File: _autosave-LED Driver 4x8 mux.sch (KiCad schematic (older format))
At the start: 23 parts, among them J1 Barrel_Jack_Switch, J2 Conn_01x02_Female, J3 8P8C_Shielded_x4, Q1 IRF9358TRPBF-2x_p-channel, Q2 IRF9358TRPBF-2x_p-channel, Q3 IRF9358TRPBF-2x_p-channel, Q4 IRF9358TRPBF-2x_p-channel, U1 SN74LV138AT_D_16, U2 TC4468EOE, U3 TC4468EOE

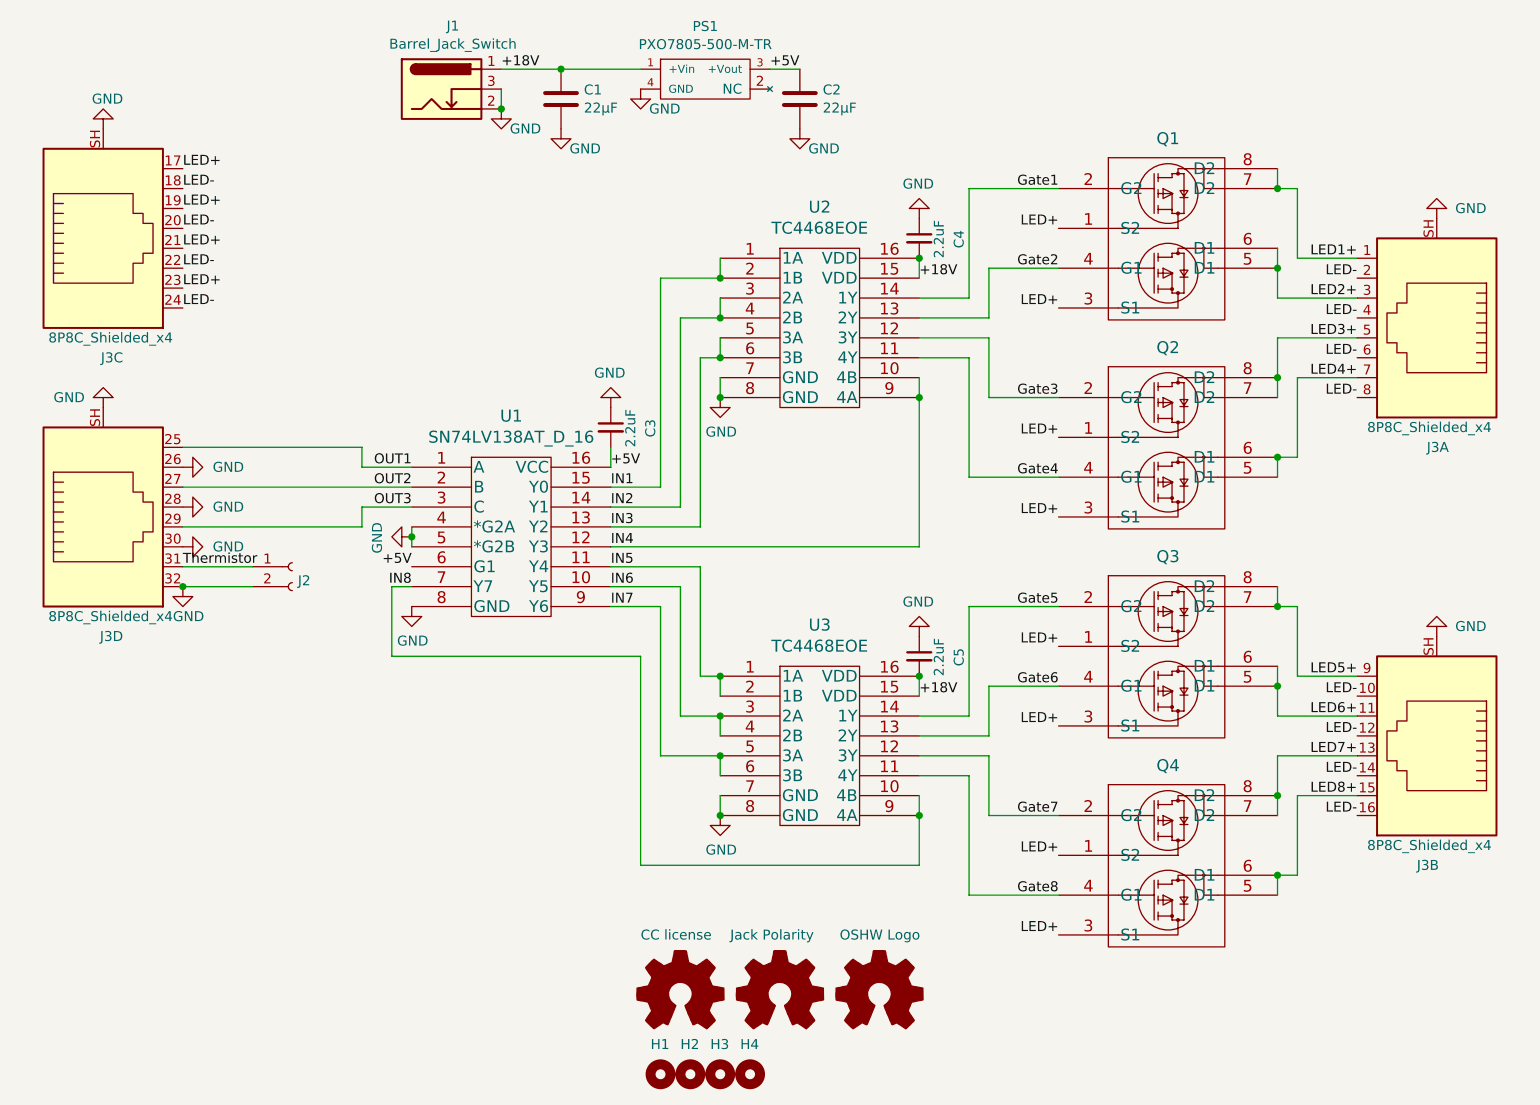
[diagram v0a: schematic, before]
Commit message: Board powered off LED river backup
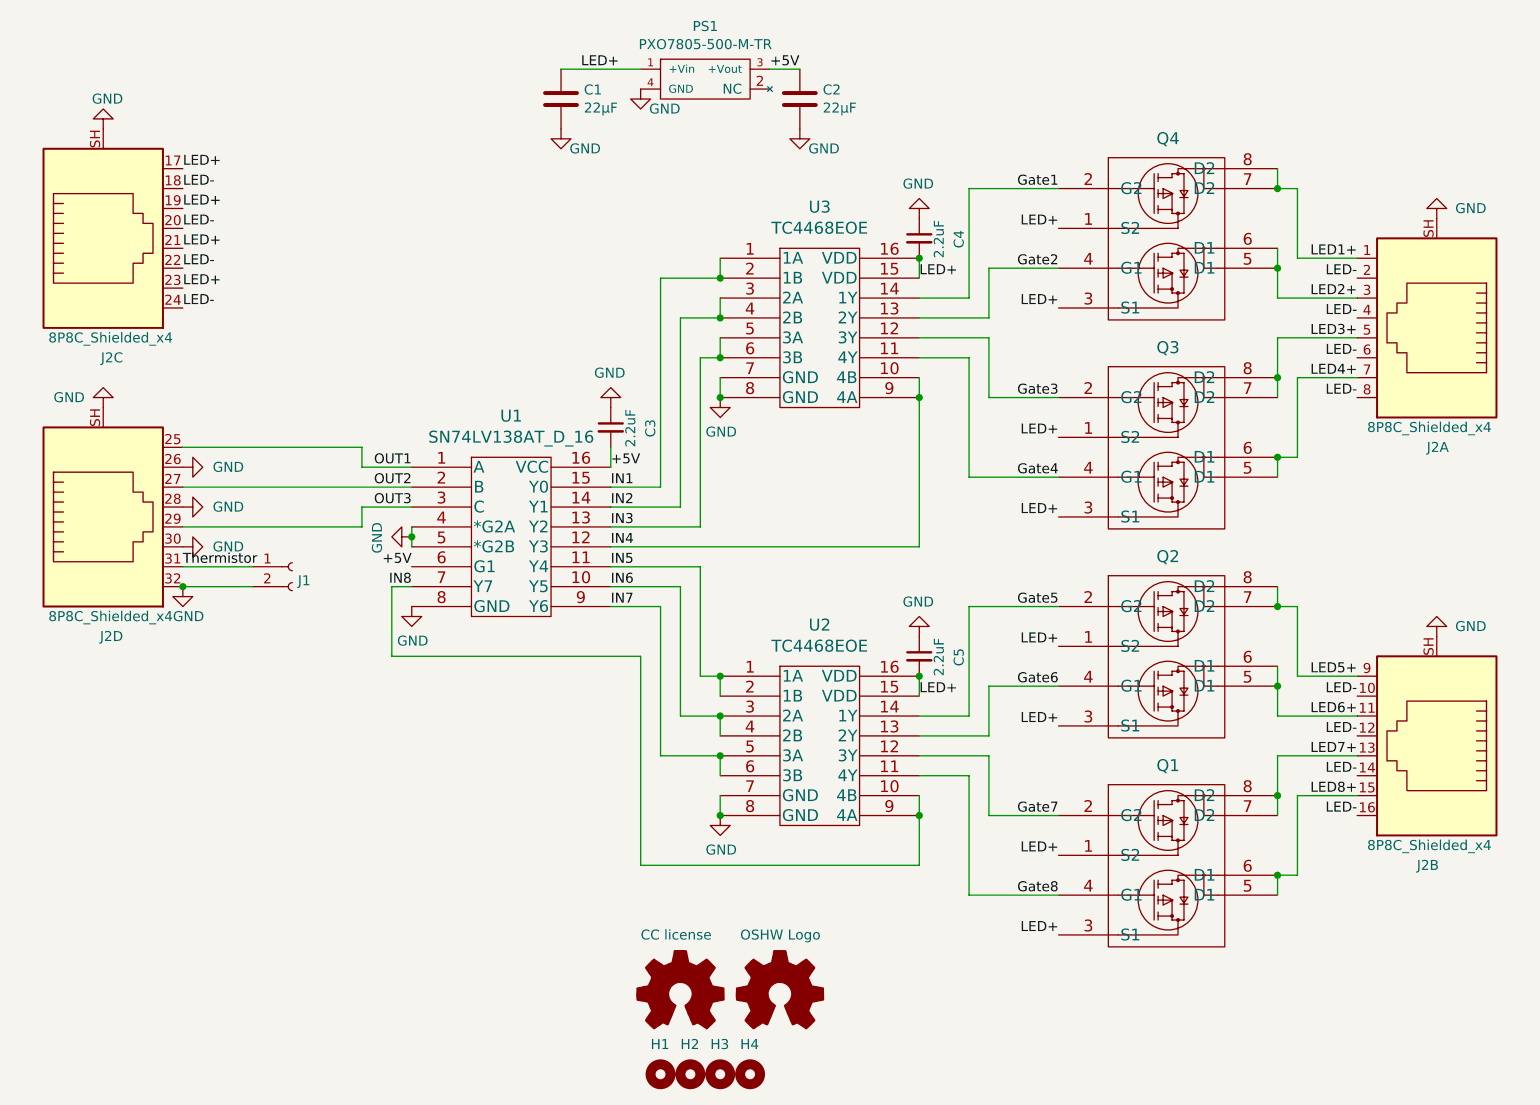
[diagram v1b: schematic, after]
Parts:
- removed J1: Barrel_Jack_Switch, Custom Footprints:DC-jack_54-00165, symbol Connector:Barrel_Jack_Switch
- removed LOGO2: Jack Polarity, Custom Footprints:Polarity_Center_Positive, symbol Graphic:Logo_Open_Hardware_Small
- J1: renamed from J2; value Conn_01x02_Female -> 2 pin header
- renumbered J3 to J2, Q4 to Q1, Q3 to Q2, Q2 to Q3, Q1 to Q4, U3 to U2, U2 to U3
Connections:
- net +18V is gone; now on net LED+: C1.1, C4.2, C5.2, PS1.1 (+Vin), U2.15 (VDD), U2.16 (VDD), U3.15 (VDD), U3.16 (VDD)
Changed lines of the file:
@@
 $EndComp
 $Comp
-L Custom_parts:8P8C_Shielded_x4 J3
+L Custom_parts:8P8C_Shielded_x4 J2
 U 4 1 5F58DBB9
 P 1150 5000
-F 0 "J3" H 1250 5650 50  0000 R CNN
+F 0 "J2" H 1250 5650 50  0000 R CNN
 F 1 "8P8C_Shielded_x4" H 1500 5550 50  0000 R CNN
 F 2 "Custom Footprints:RJ45_x4-RJSSE-5380-04" V 1150 5025 50  0001 C CNN
@@
 $EndComp
 $Comp
-L Custom_parts:8P8C_Shielded_x4 J3
+L Custom_parts:8P8C_Shielded_x4 J2
 U 3 1 5F57B5E3
 P 1150 3600
-F 0 "J3" H 1250 4250 50  0000 R CNN
+F 0 "J2" H 1250 4250 50  0000 R CNN
 F 1 "8P8C_Shielded_x4" H 1500 4150 50  0000 R CNN
 F 2 "Custom Footprints:RJ45_x4-RJSSE-5380-04" V 1150 3625 50  0001 C CNN
@@
 $EndComp
 $Comp
-L Custom_parts:8P8C_Shielded_x4 J3
+L Custom_parts:8P8C_Shielded_x4 J2
 U 2 1 5F589234
 P 7850 6150
-F 0 "J3" H 7950 6800 50  0000 R CNN
+F 0 "J2" H 7950 6800 50  0000 R CNN
 F 1 "8P8C_Shielded_x4" H 8200 6700 50  0000 R CNN
 F 2 "Custom Footprints:RJ45_x4-RJSSE-5380-04" V 7850 6175 50  0001 C CNN
@@
 $EndComp
 $Comp
-L Graphic:Logo_Open_Hardware_Small LOGO2
-U 1 1 5FF6ADDD
+L Graphic:Logo_Open_Hardware_Small LOGO3
+U 1 1 5FF6B1EE
 P 4550 7450
-F 0 "LOGO2" H 4550 7725 50  0001 C CNN
-F 1 "Jack Polarity" H 4300 7750 50  0000 L CNN
-F 2 "Custom Footprints:Polarity_Center_Positive" H 4550 7450 50  0001 C CNN
+F 0 "LOGO3" H 4550 7725 50  0001 C CNN
+F 1 "OSHW Logo" H 4350 7750 50  0000 L CNN
+F 2 "Symbol:OSHW-Logo2_7.3x6mm_SilkScreen" H 4550 7450 50  0001 C CNN
 F 3 "~" H 4550 7450 50  0001 C CNN
 	1    4550 7450
@@
 $EndComp
 $Comp
-L Graphic:Logo_Open_Hardware_Small LOGO3
-U 1 1 5FF6B1EE
-P 5050 7450
-F 0 "LOGO3" H 5050 7725 50  0001 C CNN
-F 1 "OSHW Logo" H 4850 7750 50  0000 L CNN
-F 2 "Symbol:OSHW-Logo2_7.3x6mm_SilkScreen" H 5050 7450 50  0001 C CNN
-F 3 "~" H 5050 7450 50  0001 C CNN
-	1    5050 7450
-	1    0    0    -1
-$EndComp
-$Comp
-L Custom_parts:8P8C_Shielded_x4 J3
+L Custom_parts:8P8C_Shielded_x4 J2
 U 1 1 5F5922AC
 P 7850 4050
-F 0 "J3" H 7900 4700 50  0000 R CNN
+F 0 "J2" H 7900 4700 50  0000 R CNN
 F 1 "8P8C_Shielded_x4" H 8200 4600 50  0000 R CNN
 F 2 "Custom Footprints:RJ45_x4-RJSSE-5380-04" V 7850 4075 50  0001 C CNN
@@
 	-1   0    0    1
 $EndComp
-Connection ~ 3150 3000
-Wire Wire Line
-	3150 2900 3150 3000
-$Comp
-L power:GND #PWR0108
-U 1 1 61A65F9D
-P 3150 3000
-F 0 "#PWR0108" H 3150 2750 50  0001 C CNN
-F 1 "GND" H 3350 2900 50  0000 R CNN
-F 2 "" H 3150 3000 50  0001 C CNN
-F 3 "" H 3150 3000 50  0001 C CNN
-	1    3150 3000
-	1    0    0    -1
-$EndComp
-$Comp
-L Connector:Barrel_Jack_Switch J1
-U 1 1 61A65FA5
-P 2850 2900
-F 0 "J1" H 2907 3217 50  0000 C CNN
-F 1 "Barrel_Jack_Switch" H 2907 3126 50  0000 C CNN
-F 2 "Custom Footprints:DC-jack_54-00165" H 2900 2860 50  0001 C CNN
-F 3 "https://tensility.s3-us-west-2.amazonaws.com/uploads/product_doc/document/4054/54-00165.pdf" H 2900 2860 50  0001 C CNN
-F 4 "Tensility International Corp" H 2850 2900 50  0001 C CNN "Manufacturer"
-F 5 "54-00165" H 2850 2900 50  0001 C CNN "Part #"
-	1    2850 2900
-	1    0    0    -1
-$EndComp
-Text Label 3150 2800 0    50   ~ 0
-+18V
 $Comp
 L power:GND #PWR015
@@
 $EndComp
 Wire Wire Line
-	3150 2800 3450 2800
-Wire Wire Line
 	3450 2800 3850 2800
-Connection ~ 3450 2800
 $Comp
 L power:GND #PWR0102
@@
 $EndComp
 $Comp
-L Custom_parts:TC4468EOE U2
+L Custom_parts:TC4468EOE U3
 U 1 1 64F06EE9
 P 4250 3750
-F 0 "U2" H 4750 4007 60  0000 C CNN
+F 0 "U3" H 4750 4007 60  0000 C CNN
 F 1 "TC4468EOE" H 4750 3901 60  0000 C CNN
 F 2 "Custom Footprints:TC4468EOE" H 5350 3990 60  0001 C CNN
@@
 Wire Wire Line
 	5250 5950 5250 5850
-Text Label 5250 3850 0    50   ~ 0
-+18V
-Text Label 5250 5950 0    50   ~ 0
-+18V
 Wire Wire Line
 	4250 6450 4250 6550
@@
 $EndComp
 $Comp
-L Custom_parts:IRF9358TRPBF-2x_p-channel Q1
+L Custom_parts:IRF9358TRPBF-2x_p-channel Q4
 U 1 1 64F4537D
 P 7450 3000
-F 0 "Q1" H 6500 2851 60  0000 C CNN
+F 0 "Q4" H 6500 2851 60  0000 C CNN
 F 1 "IRF9358TRPBF-2x_p-channel" H 6500 2875 60  0001 C CNN
 F 2 "Custom Footprints:IRF9358TRPBF-2x_p-channel" H 6500 2815 60  0001 C CNN
@@
 Gate8
 $Comp
-L Custom_parts:IRF9358TRPBF-2x_p-channel Q2
+L Custom_parts:IRF9358TRPBF-2x_p-channel Q3
 U 1 1 64F7C414
 P 7450 4050
-F 0 "Q2" H 6500 3901 60  0000 C CNN
+F 0 "Q3" H 6500 3901 60  0000 C CNN
 F 1 "IRF9358TRPBF-2x_p-channel" H 6500 3925 60  0001 C CNN
 F 2 "Custom Footprints:IRF9358TRPBF-2x_p-channel" H 6500 3865 60  0001 C CNN
@@
 $EndComp
 $Comp
-L Custom_parts:IRF9358TRPBF-2x_p-channel Q3
+L Custom_parts:IRF9358TRPBF-2x_p-channel Q2
 U 1 1 64F7E6DD
 P 7450 5100
-F 0 "Q3" H 6500 4951 60  0000 C CNN
+F 0 "Q2" H 6500 4951 60  0000 C CNN
 F 1 "IRF9358TRPBF-2x_p-channel" H 6500 4975 60  0001 C CNN
 F 2 "Custom Footprints:IRF9358TRPBF-2x_p-channel" H 6500 4915 60  0001 C CNN
@@
 $EndComp
 $Comp
-L Custom_parts:IRF9358TRPBF-2x_p-channel Q4
+L Custom_parts:IRF9358TRPBF-2x_p-channel Q1
 U 1 1 64F81FE0
 P 7450 6150
-F 0 "Q4" H 6500 6001 60  0000 C CNN
+F 0 "Q1" H 6500 6001 60  0000 C CNN
 F 1 "IRF9358TRPBF-2x_p-channel" H 6500 6025 60  0001 C CNN
 F 2 "Custom Footprints:IRF9358TRPBF-2x_p-channel" H 6500 5965 60  0001 C CNN
@@
 $EndComp
 $Comp
-L Custom_parts:TC4468EOE U3
+L Custom_parts:TC4468EOE U2
 U 1 1 64F8812A
 P 4250 5850
-F 0 "U3" H 4750 6107 60  0000 C CNN
+F 0 "U2" H 4750 6107 60  0000 C CNN
 F 1 "TC4468EOE" H 4750 6001 60  0000 C CNN
 F 2 "Custom Footprints:TC4468EOE" H 5350 6090 60  0001 C CNN
@@
 $EndComp
 $Comp
-L Connector:Conn_01x02_Female J2
+L Connector:Conn_01x02_Female J1
 U 1 1 64F692B9
 P 2100 5300
-F 0 "J2" H 2128 5230 50  0000 L CNN
-F 1 "Conn_01x02_Female" H 2128 5185 50  0001 L CNN
+F 0 "J1" H 2128 5230 50  0000 L CNN
+F 1 "2 pin header" H 2128 5185 50  0001 L CNN
 F 2 "Connector_PinSocket_2.54mm:PinSocket_1x02_P2.54mm_Vertical_SMD_Pin1Right" H 2100 5300 50  0001 C CNN
-F 3 "~" H 2100 5300 50  0001 C CNN
+F 3 "https://cdn.amphenol-icc.com/media/wysiwyg/files/drawing/rjsse538004.pdf" H 2100 5300 50  0001 C CNN
 	1    2100 5300
 	1    0    0    -1
@@
 Wire Wire Line
 	1550 5300 1900 5300
+Text Label 3550 2800 0    50   ~ 0
+LED+
+Text Label 5250 3850 0    50   ~ 0
+LED+
+Text Label 5250 5950 0    50   ~ 0
+LED+
 $EndSCHEMATC
